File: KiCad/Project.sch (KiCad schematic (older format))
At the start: 11 parts, among them IC1 ATMEGA328-P, P1 CONN_02X03, P2 CONN_01X02, SW4 SW_PUSH, U1 BlueSmirf, Y1 Crystal

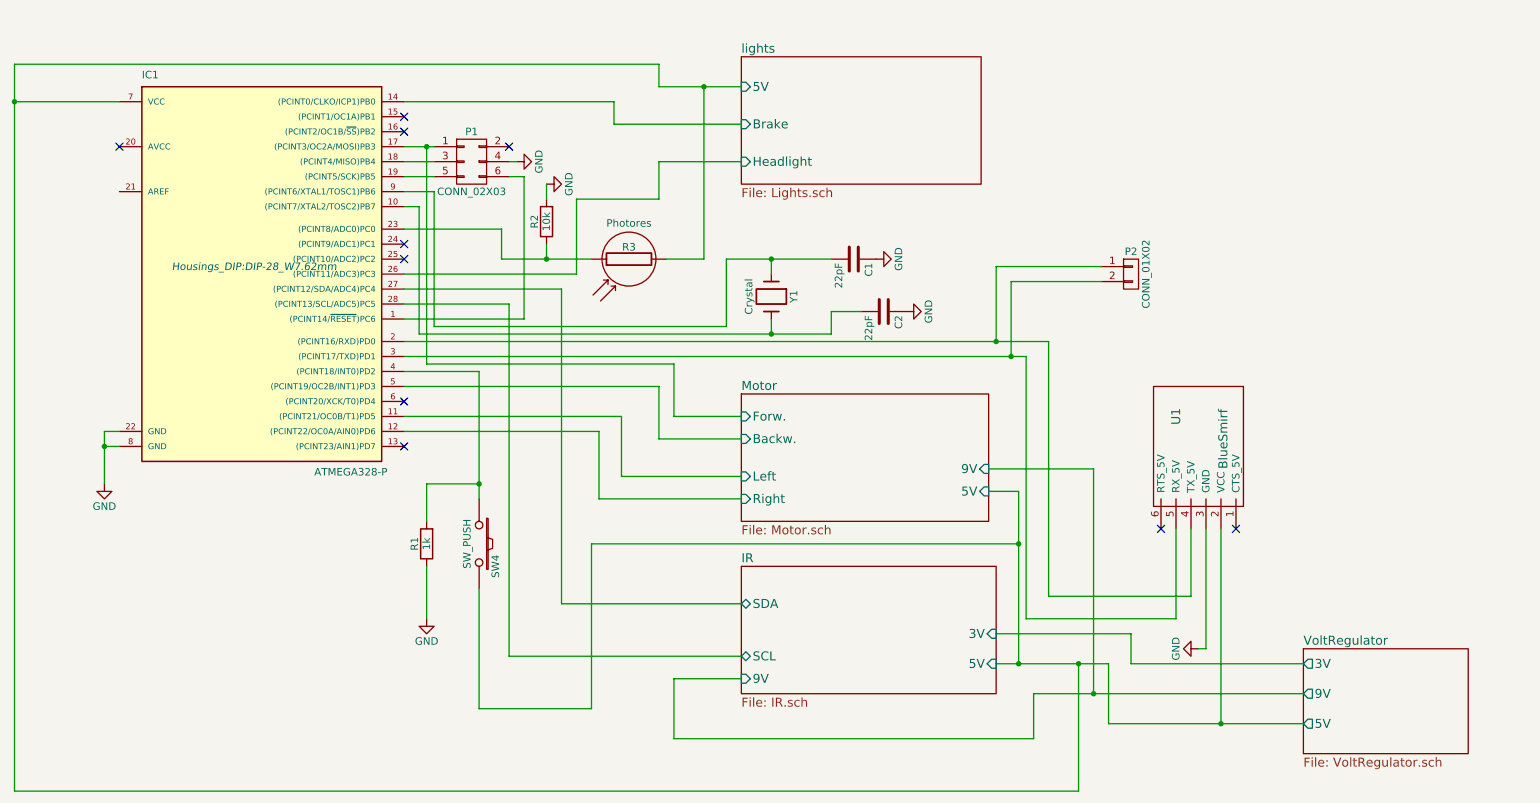
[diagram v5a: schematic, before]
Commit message: Updated the pcb to smaller size and footprints
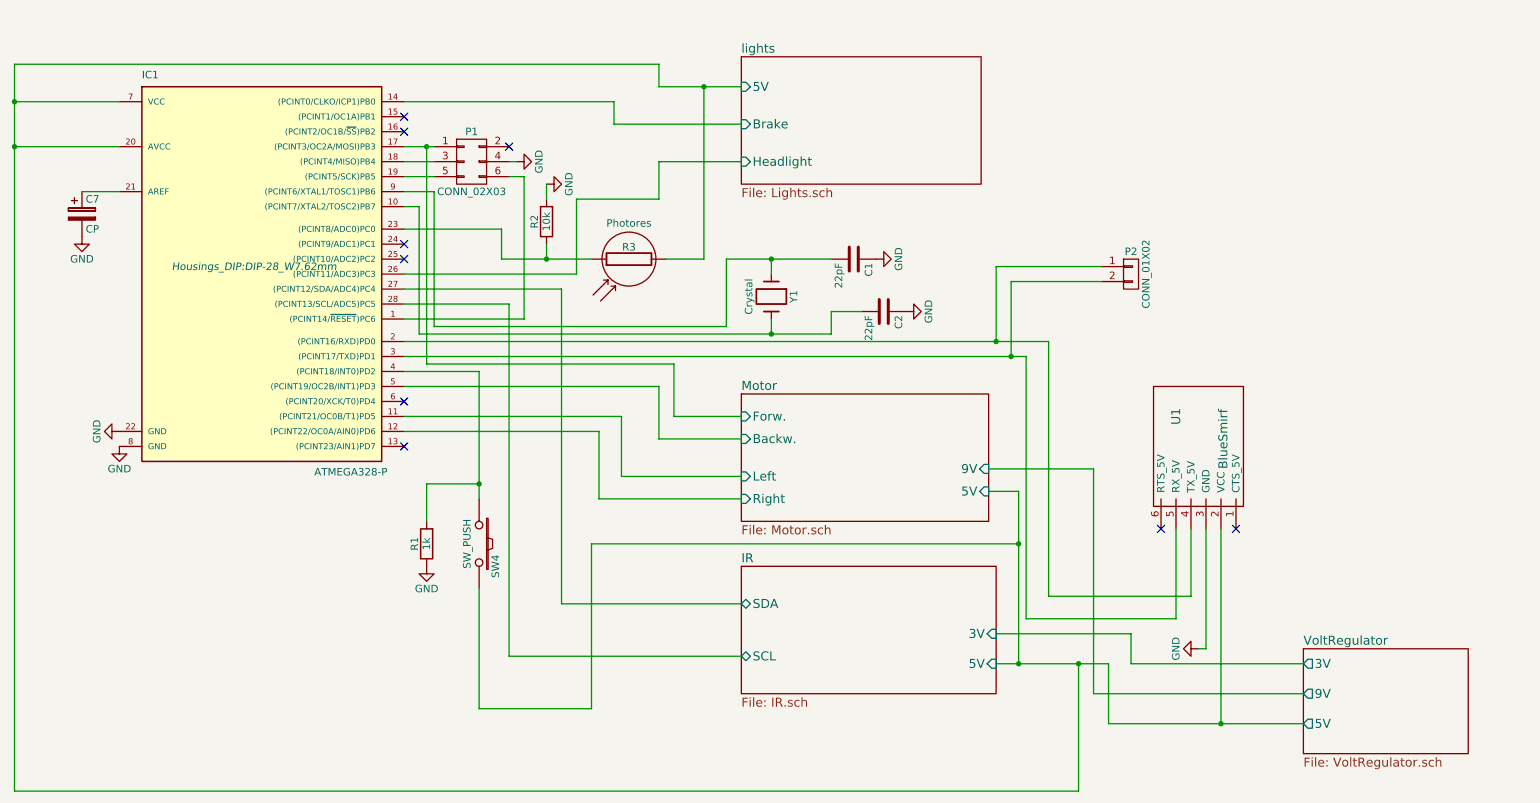
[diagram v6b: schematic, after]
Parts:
- added C7: CP, Capacitors_ThroughHole:C_Radial_D5_L6_P2.5, symbol CP
- R3, SW4: footprint Wire_Pads:SolderWirePad_2x_1mmDrill -> Holes:SolderWirePad1mmmodified
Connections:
- net GND: now also C7.2
- net IR/5V: now also IC1.20 (AVCC)
- net at IC1.21 (AREF): now also C7.1
- no-connect marks 10 -> 9
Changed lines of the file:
@@
 L GND #PWR01
 U 1 1 5715DC43
-P 1500 3800
-F 0 "#PWR01" H 1500 3550 50  0001 C CNN
-F 1 "GND" H 1500 3650 50  0000 C CNN
-F 2 "" H 1500 3800 50  0000 C CNN
-F 3 "" H 1500 3800 50  0000 C CNN
-	1    1500 3800
-	1    0    0    -1
-$EndComp
-Wire Wire Line
-	1600 3450 1500 3450
-Wire Wire Line
-	1500 3450 1500 3800
-Wire Wire Line
-	1600 3550 1500 3550
-Connection ~ 1500 3550
+P 1600 3550
+F 0 "#PWR01" H 1600 3300 50  0001 C CNN
+F 1 "GND" H 1600 3400 50  0000 C CNN
+F 2 "" H 1600 3550 50  0000 C CNN
+F 3 "" H 1600 3550 50  0000 C CNN
+	1    1600 3550
+	1    0    0    -1
+$EndComp
 $Sheet
 S 9500 4900 1100 700
@@
 F3 "SDA" B L 5750 4600 60
 F4 "SCL" B L 5750 4950 60
-F5 "9V" I L 5750 5100 60
-F6 "3V" I R 7450 4800 60
+F5 "3V" I R 7450 4800 60
 $EndSheet
 Wire Wire Line
@@
 F 0 "R3" V 5080 2300 50  0000 C CNN
 F 1 "Photores" V 5210 2300 50  0000 C TNN
-F 2 "Wire_Pads:SolderWirePad_2x_1mmDrill" V 4930 2300 50  0001 C CNN
+F 2 "Holes:SolderWirePad1mmmodified" V 4930 2300 50  0001 C CNN
 F 3 "" H 5000 2300 50  0000 C CNN
 	1    5000 2300
@@
 Wire Wire Line
 	8350 4800 7450 4800
-Wire Wire Line
-	9500 5200 7700 5200
-Wire Wire Line
-	7700 5200 7700 5500
-Wire Wire Line
-	7700 5500 5300 5500
-Wire Wire Line
-	5300 5500 5300 5100
-Wire Wire Line
-	5300 5100 5750 5100
 Wire Wire Line
 	4450 1800 4450 1900
@@
 Wire Wire Line
 	8100 3700 7400 3700
-Connection ~ 8100 5200
 $Comp
 L Crystal Y1
@@
 F 0 "SW4" H 4150 4310 50  0000 C CNN
 F 1 "SW_PUSH" H 4000 4120 50  0000 C CNN
-F 2 "Wire_Pads:SolderWirePad_2x_1mmDrill" H 4000 4200 50  0001 C CNN
+F 2 "Holes:SolderWirePad1mmmodified" H 4000 4200 50  0001 C CNN
 F 3 "" H 4000 4200 50  0000 C CNN
 	1    4000 4200
@@
 L GND #PWR07
 U 1 1 5734269F
-P 3650 4700
-F 0 "#PWR07" H 3650 4450 50  0001 C CNN
-F 1 "GND" H 3650 4550 50  0000 C CNN
-F 2 "" H 3650 4700 50  0000 C CNN
-F 3 "" H 3650 4700 50  0000 C CNN
-	1    3650 4700
+P 3650 4350
+F 0 "#PWR07" H 3650 4100 50  0001 C CNN
+F 1 "GND" H 3650 4200 50  0000 C CNN
+F 2 "" H 3650 4350 50  0000 C CNN
+F 3 "" H 3650 4350 50  0000 C CNN
+	1    3650 4350
 	1    0    0    -1
 $EndComp
@@
 	3650 3800 3650 4050
 Connection ~ 4000 3800
-Wire Wire Line
-	3650 4350 3650 4700
 Wire Wire Line
 	5750 1400 4900 1400
@@
 NoConn ~ 3500 3250
 NoConn ~ 3500 3550
-NoConn ~ 1600 1550
+$Comp
+L CP C7
+U 1 1 573CD334
+P 1350 2000
+F 0 "C7" H 1375 2100 50  0000 L CNN
+F 1 "CP" H 1375 1900 50  0000 L CNN
+F 2 "Capacitors_ThroughHole:C_Radial_D5_L6_P2.5" H 1388 1850 50  0001 C CNN
+F 3 "" H 1350 2000 50  0000 C CNN
+	1    1350 2000
+	1    0    0    -1
+$EndComp
+Wire Wire Line
+	1350 1850 1600 1850
+$Comp
+L GND #PWR08
+U 1 1 573CD768
+P 1350 2150
+F 0 "#PWR08" H 1350 1900 50  0001 C CNN
+F 1 "GND" H 1350 2000 50  0000 C CNN
+F 2 "" H 1350 2150 50  0000 C CNN
+F 3 "" H 1350 2150 50  0000 C CNN
+	1    1350 2150
+	1    0    0    -1
+$EndComp
+Wire Wire Line
+	1600 1550 900  1550
+Connection ~ 900  1550
+Wire Wire Line
+	9500 5200 8100 5200
+$Comp
+L GND #PWR09
+U 1 1 573E0A60
+P 1600 3450
+F 0 "#PWR09" H 1600 3200 50  0001 C CNN
+F 1 "GND" H 1600 3300 50  0000 C CNN
+F 2 "" H 1600 3450 50  0000 C CNN
+F 3 "" H 1600 3450 50  0000 C CNN
+	1    1600 3450
+	0    1    1    0
+$EndComp
 $EndSCHEMATC
